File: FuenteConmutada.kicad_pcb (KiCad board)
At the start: 2 copper layers, 50 x 50 mm, 21 parts, among them J1 Conn_01x02_Socket, J2 Conn_01x03_Socket, U1 MT3608

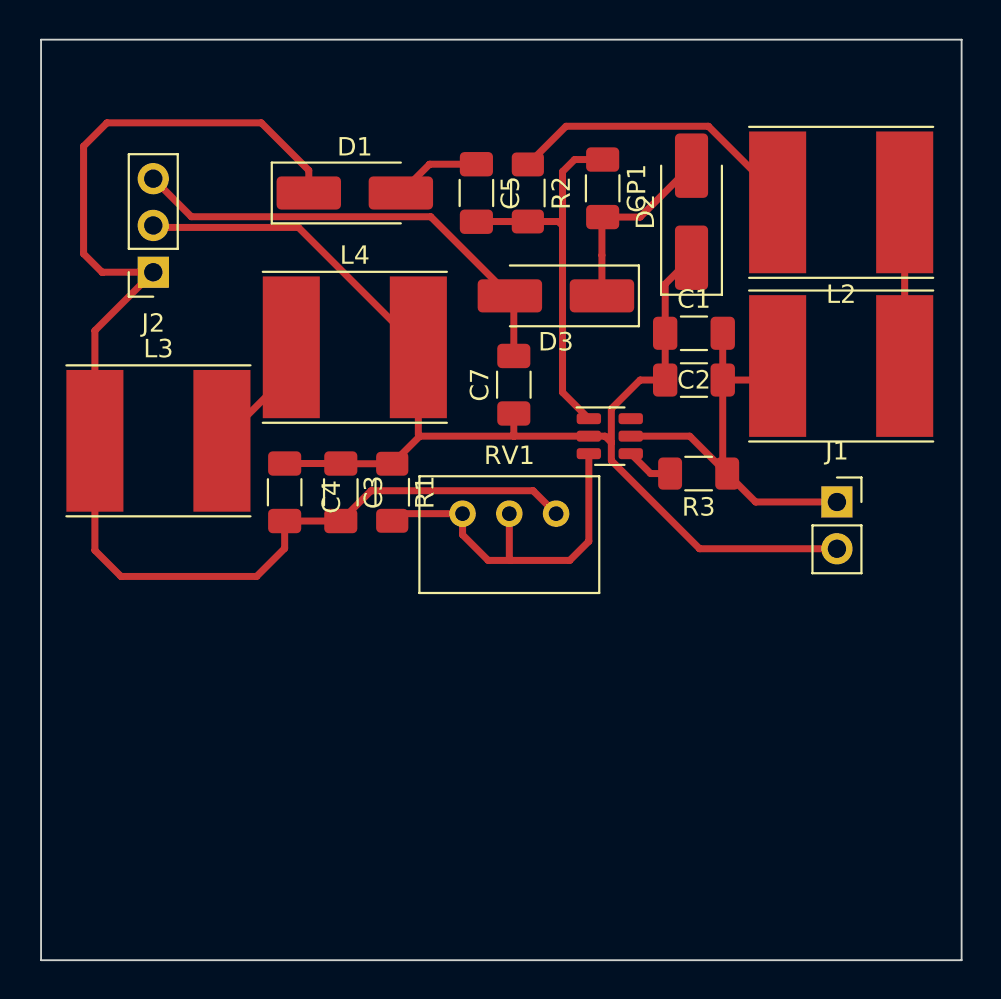
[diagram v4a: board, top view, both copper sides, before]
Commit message: Cambios PCB+Esquematico
Huellas nuevas para inductores, diodos.
Correccion de diodo mal ubicado.
Se añadio R en serie con inductores 3 y 4, capacitor para compensacion, un segundo capacitor para salida Vo-.
Planos de GND, Vin, Vo+ y Vo-. Y tambien se agrandaron algunas pistas.
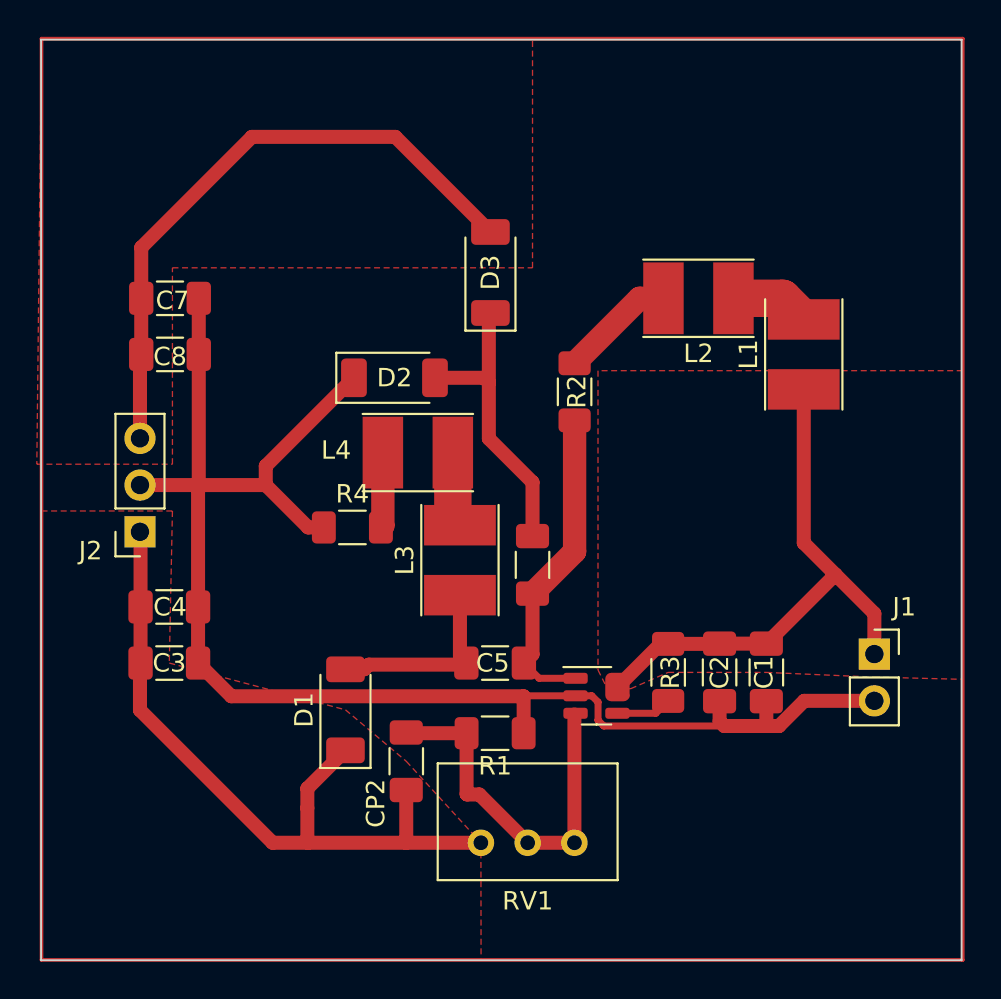
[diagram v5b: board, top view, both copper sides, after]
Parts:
- added C8: 22uF, Capacitor_SMD:C_1206_3216Metric_Pad1.33x1.80mm_HandSolder, F.Cu at (72.0, 93.1)
- added CP2: 22uF, Capacitor_SMD:C_1206_3216Metric_Pad1.33x1.80mm_HandSolder, F.Cu at (84.8, 115.2)
- added R4: R, Resistor_SMD:R_1206_3216Metric_Pad1.30x1.75mm_HandSolder, F.Cu at (81.9, 102.5)
- D1, D2, D3: footprint Diode_SMD:D_SMA_Handsoldering -> Diode_SMD:D_SOD-128
- L1, L2, L3, L4: footprint Inductor_SMD:L_Taiyo-Yuden_NR-80xx_HandSoldering -> Inductor_SMD:L_Taiyo-Yuden_NR-40xx_HandSoldering
- moved D1 28.1 mm to (81.5, 112.4), turned to 90 degrees
- moved C5 25.6 mm to (89.7, 109.9), turned to 0 degrees
- moved CP1 20.8 mm to (91.7, 104.5), turned to 90 degrees
- moved C7 19.3 mm to (72.0, 90.0), turned to 180 degrees
- moved C1 18.8 mm to (104.4, 110.4), turned to 90 degrees
- moved D2 18.5 mm to (84.2, 94.4), turned to 0 degrees
- moved RV1 18.3 mm to (88.9, 119.6), turned to 180 degrees
- moved L3 17.6 mm to (87.8, 104.3), turned to 90 degrees
- moved C2 15.9 mm to (101.9, 110.4), turned to 90 degrees
- moved R1 14.2 mm to (89.7, 113.7), turned to 0 degrees
- moved J2 14.1 mm to (70.4, 102.7)
- moved U1 14.1 mm to (95.2, 111.6)
- moved C3 13.1 mm to (72.0, 109.9), turned to 180 degrees
- moved R2 11.1 mm to (94.0, 95.1)
- moved R3 10.9 mm to (99.1, 110.4), turned to -90 degrees
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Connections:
- L3 pad 1: /Vo+ -> Net-(D1-A)
- L4 pad 2: GND -> Net-(L4-Pad2)
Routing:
- net /Vo+: track 70.5 -> 40.0 mm
- net GND: track 69.6 -> 82.8 mm
- net Net-(L2-Pad2): track 18.7 -> 6.29 mm
- net /Vo-: track 25.4 -> 34.0 mm
- net /Vin: track 23.4 -> 30.8 mm
- net Net-(D1-A): track 4.75 -> 10.5 mm
- net Net-(D2-A): track 10.5 -> 16.2 mm
- net Net-(L1-Pad2): track 8.89 -> 4.30 mm
- net Net-(L4-Pad2): track 0.00 -> 4.11 mm
- net Net-(L3-Pad2): track 7.95 -> 4.10 mm
- net Net-(U1-SW): track 21.2 -> 17.5 mm
- net Net-(U1-FB): track 19.8 -> 20.6 mm
- added copper zone on F.Cu, net /Vin
- added copper zone on F.Cu, net /Vo+
- added copper zone on F.Cu, net /Vo-
- added copper zone on F.Cu, net GND

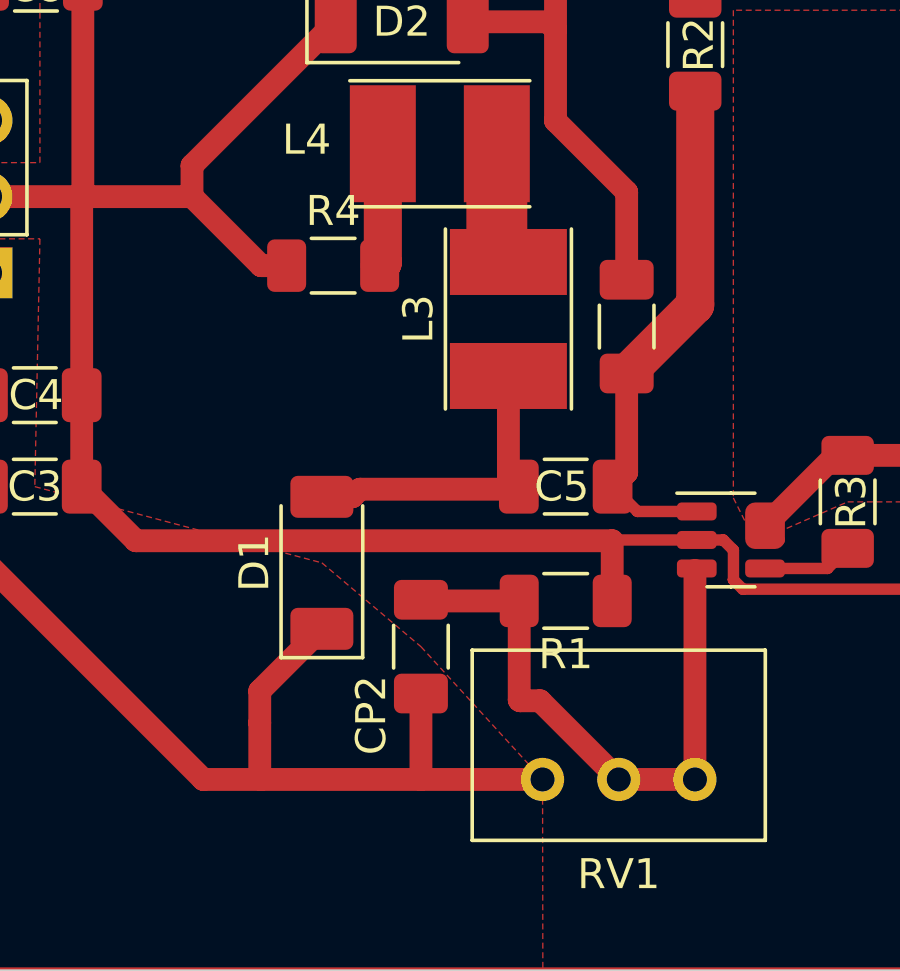
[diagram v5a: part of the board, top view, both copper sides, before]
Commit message: PCB+Esquematico(actualizacion)
Se agrego R en serie con el diodo D1.
Y se habia agregado anteriormente una modificación sobre la huella del regulador.
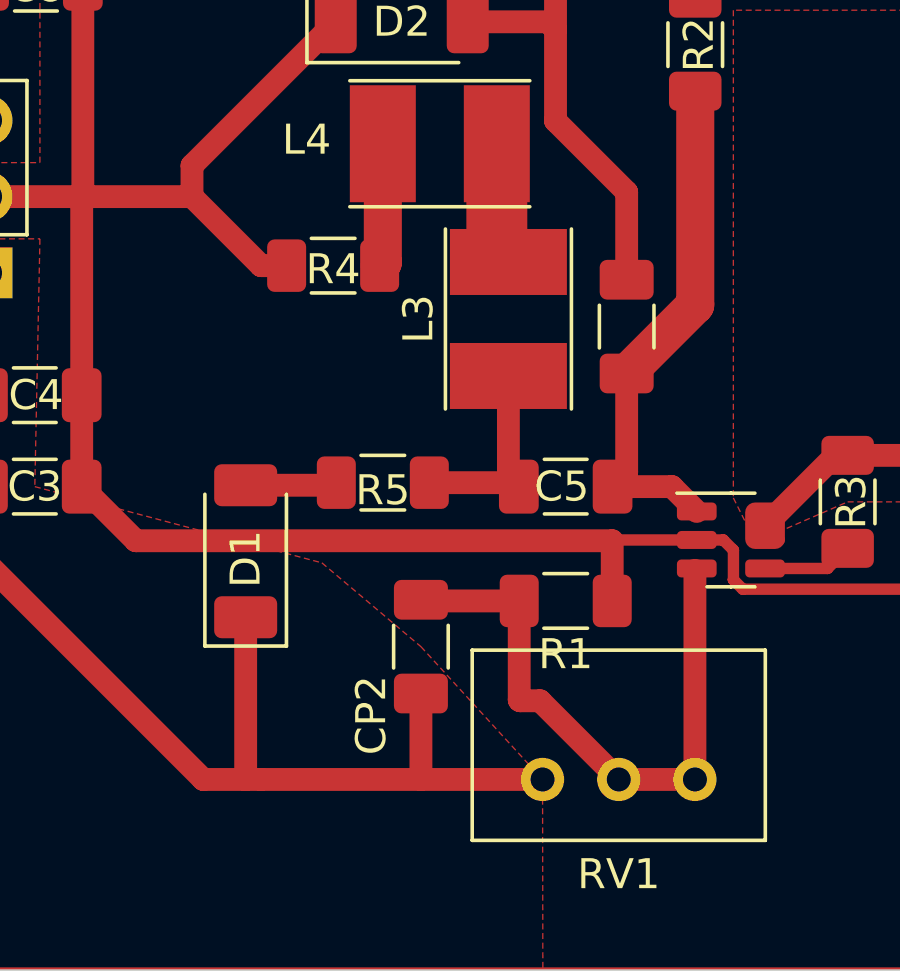
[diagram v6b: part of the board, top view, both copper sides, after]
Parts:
- added R5: R, Resistor_SMD:R_1206_3216Metric_Pad1.30x1.75mm_HandSolder, F.Cu at (83.6, 109.7)
- moved D1 2.57 mm to (79.0, 112.0)
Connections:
- C5 pad 1: Net-(D1-A) -> Net-(C5-Pad1)
- L3 pad 1: Net-(D1-A) -> Net-(C5-Pad1)
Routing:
- net Net-(D1-A): track 10.5 -> 3.06 mm
- net Net-(C5-Pad1): track 0.00 -> 6.99 mm
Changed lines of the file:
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@@
   (net 12 "Net-(L3-Pad2)")
   (net 13 "Net-(L4-Pad2)")
+  (net 14 "Net-(C5-Pad1)")
   (footprint "Capacitor_SMD:C_1206_3216Metric_Pad1.33x1.80mm_HandSolder" (layer "F.Cu")
     (at 91.694 104.526 90)
@@
     (property "ki_keywords" "R res resistor")
     (attr smd)
-    (fp_text reference "R4" (at 0 -1.82) (layer "F.SilkS")
+    (fp_text reference "R4" (at 0 0.122) (layer "F.SilkS")
         (effects (font (size 1 1) (thickness 0.15)))
     )
     (fp_text value "R" (at 0 1.82) (layer "F.Fab")
         (effects (font (size 1 1) (thickness 0.15)))
-    )
-    (fp_text user "${REFERENCE}" (at 0 0) (layer "F.Fab")
-        (effects (font (size 0.8 0.8) (thickness 0.12)))
     )
     (fp_line (start -0.727064 -0.91) (end 0.727064 -0.91)
@@
       (stroke (width 0.1) (type solid)) (layer "F.Fab"))
     (pad "1" smd rect (at -1.9 0 90) (size 2.2 3.9) (layers "F.Cu" "F.Paste" "F.Mask")
-      (net 3 "Net-(D1-A)") (pinfunction "1") (pintype "passive"))
+      (net 14 "Net-(C5-Pad1)") (pinfunction "1") (pintype "passive"))
     (pad "2" smd rect (at 1.9 0 90) (size 2.2 3.9) (layers "F.Cu" "F.Paste" "F.Mask")
       (net 12 "Net-(L3-Pad2)") (pinfunction "2") (pintype "passive"))
@@
   )
   (footprint "Diode_SMD:D_SOD-128" (layer "F.Cu")
-    (at 81.534 112.4 90)
+    (at 78.994 112.014 90)
     (descr "D_SOD-128 (CFP5 SlimSMAW), https://assets.nexperia.com/documents/outline-drawing/SOD128.pdf")
     (tags "D_SOD-128")
@@
     (property "ki_keywords" "diode Schottky")
     (attr smd)
-    (fp_text reference "D1" (at 0 -2.25 90) (layer "F.SilkS")
+    (fp_text reference "D1" (at -0.254 0 90) (layer "F.SilkS")
         (effects (font (size 1 1) (thickness 0.15)))
     )
@@
       (stroke (width 0.1) (type solid)) (layer "F.Fab"))
     (pad "1" smd roundrect (at -1.5625 0) (size 1.325 1.8) (layers "F.Cu" "F.Paste" "F.Mask") (roundrect_rratio 0.188679)
-      (net 3 "Net-(D1-A)") (pintype "passive"))
+      (net 14 "Net-(C5-Pad1)") (pintype "passive"))
     (pad "2" smd roundrect (at 1.5625 0) (size 1.325 1.8) (layers "F.Cu" "F.Paste" "F.Mask") (roundrect_rratio 0.188679)
       (net 7 "Net-(U1-SW)") (pintype "passive"))
@@
     (pad "2" smd roundrect (at 1.55 0 270) (size 1.3 1.75) (layers "F.Cu" "F.Paste" "F.Mask") (roundrect_rratio 0.192308)
       (net 2 "Net-(U1-EN)") (pintype "passive"))
+    (model "${KICAD6_3DMODEL_DIR}/Resistor_SMD.3dshapes/R_1206_3216Metric.wrl"
+      (offset (xyz 0 0 0))
+      (scale (xyz 1 1 1))
+      (rotate (xyz 0 0 0))
+    )
+  )
+  (footprint "Resistor_SMD:R_1206_3216Metric_Pad1.30x1.75mm_HandSolder" (layer "F.Cu")
+    (at 83.566 109.728 180)
+    (descr "Resistor SMD 1206 (3216 Metric), square (rectangular) end terminal, IPC_7351 nominal with elongated pad for handsoldering. (Body size source: IPC-SM-782 page 72, https://www.pcb-3d.com/wordpress/wp-content/uploads/ipc-sm-782a_amendment_1_and_2.pdf), generated with kicad-footprint-generator")
+    (tags "resistor handsolder")
+    (property "Sheetfile" "FuenteConmutada.kicad_sch")
+    (property "Sheetname" "")
+    (property "ki_description" "Resistor")
+    (property "ki_keywords" "R res resistor")
+    (attr smd)
+    (fp_text reference "R5" (at 0 -0.254) (layer "F.SilkS")
+        (effects (font (size 1 1) (thickness 0.15)))
+    )
+    (fp_text value "R" (at 0 1.82) (layer "F.Fab")
+        (effects (font (size 1 1) (thickness 0.15)))
+    )
+    (fp_line (start -0.727064 -0.91) (end 0.727064 -0.91)
+      (stroke (width 0.12) (type solid)) (layer "F.SilkS"))
+    (fp_line (start -0.727064 0.91) (end 0.727064 0.91)
+      (stroke (width 0.12) (type solid)) (layer "F.SilkS"))
+    (fp_line (start -2.45 -1.12) (end 2.45 -1.12)
+      (stroke (width 0.05) (type solid)) (layer "F.CrtYd"))
+    (fp_line (start -2.45 1.12) (end -2.45 -1.12)
+      (stroke (width 0.05) (type solid)) (layer "F.CrtYd"))
+    (fp_line (start 2.45 -1.12) (end 2.45 1.12)
+      (stroke (width 0.05) (type solid)) (layer "F.CrtYd"))
+    (fp_line (start 2.45 1.12) (end -2.45 1.12)
+      (stroke (width 0.05) (type solid)) (layer "F.CrtYd"))
+    (fp_line (start -1.6 -0.8) (end 1.6 -0.8)
+      (stroke (width 0.1) (type solid)) (layer "F.Fab"))
+    (fp_line (start -1.6 0.8) (end -1.6 -0.8)
+      (stroke (width 0.1) (type solid)) (layer "F.Fab"))
+    (fp_line (start 1.6 -0.8) (end 1.6 0.8)
+      (stroke (width 0.1) (type solid)) (layer "F.Fab"))
+    (fp_line (start 1.6 0.8) (end -1.6 0.8)
+      (stroke (width 0.1) (type solid)) (layer "F.Fab"))
+    (pad "1" smd roundrect (at -1.55 0 180) (size 1.3 1.75) (layers "F.Cu" "F.Paste" "F.Mask") (roundrect_rratio 0.192308)
+      (net 14 "Net-(C5-Pad1)") (pintype "passive"))
+    (pad "2" smd roundrect (at 1.55 0 180) (size 1.3 1.75) (layers "F.Cu" "F.Paste" "F.Mask") (roundrect_rratio 0.192308)
+      (net 3 "Net-(D1-A)") (pintype "passive"))
     (model "${KICAD6_3DMODEL_DIR}/Resistor_SMD.3dshapes/R_1206_3216Metric.wrl"
       (offset (xyz 0 0 0))
@@
   (segment (start 99.06 111.918) (end 98.39 112.588) (width 0.381) (layer "F.Cu") (net 2))
   (segment (start 98.39 112.588) (end 96.306 112.588) (width 0.381) (layer "F.Cu") (net 2))
-  (segment (start 82.55 110.2) (end 82.804 109.946) (width 0.762) (layer "F.Cu") (net 3))
-  (segment (start 87.752 106.172) (end 87.752 109.5125) (width 0.762) (layer "F.Cu") (net 3))
-  (segment (start 88.0995 109.86) (end 88.0135 109.946) (width 0.762) (layer "F.Cu") (net 3))
-  (segment (start 81.534 110.2) (end 82.55 110.2) (width 0.762) (layer "F.Cu") (net 3))
-  (segment (start 88.0135 109.946) (end 82.804 109.946) (width 0.762) (layer "F.Cu") (net 3))
-  (segment (start 87.752 109.5125) (end 88.0995 109.86) (width 0.762) (layer "F.Cu") (net 3))
+  (segment (start 81.93 109.814) (end 82.016 109.728) (width 0.762) (layer "F.Cu") (net 3))
+  (segment (start 78.994 109.814) (end 81.93 109.814) (width 0.762) (layer "F.Cu") (net 3))
   (segment (start 110.261 109.372) (end 110.261 107.1695) (width 0.762) (layer "F.Cu") (net 4))
   (segment (start 104.394 108.8055) (end 108.1455 105.054) (width 0.762) (layer "F.Cu") (net 4))
@@
   (segment (start 88.89 119.621) (end 84.836 119.621) (width 0.762) (layer "F.Cu") (net 5))
   (segment (start 84.836 119.621) (end 79.502 119.621) (width 0.762) (layer "F.Cu") (net 5))
-  (segment (start 79.4635 119.5825) (end 79.502 119.621) (width 0.762) (layer "F.Cu") (net 5))
+  (segment (start 78.994 119.621) (end 77.579 119.621) (width 0.762) (layer "F.Cu") (net 5))
+  (segment (start 79.502 119.621) (end 78.994 119.621) (width 0.762) (layer "F.Cu") (net 5))
   (segment (start 70.373 109.89) (end 70.403 109.86) (width 0.762) (layer "F.Cu") (net 5))
-  (segment (start 79.4635 116.6705) (end 79.4635 117.734) (width 0.762) (layer "F.Cu") (net 5))
   (segment (start 70.373 112.415) (end 77.579 119.621) (width 0.762) (layer "F.Cu") (net 5))
   (segment (start 84.836 116.7565) (end 84.836 119.621) (width 0.762) (layer "F.Cu") (net 5))
   (segment (start 70.403 102.763) (end 70.373 102.733) (width 0.762) (layer "F.Cu") (net 5))
-  (segment (start 81.534 114.6) (end 79.4635 116.6705) (width 0.762) (layer "F.Cu") (net 5))
+  (segment (start 78.994 114.214) (end 78.994 119.621) (width 0.762) (layer "F.Cu") (net 5))
   (segment (start 70.403 109.86) (end 70.403 106.812) (width 0.762) (layer "F.Cu") (net 5))
-  (segment (start 79.4635 117.734) (end 79.4635 119.5825) (width 0.762) (layer "F.Cu") (net 5))
   (segment (start 70.373 112.415) (end 70.373 109.89) (width 0.762) (layer "F.Cu") (net 5))
-  (segment (start 79.502 119.621) (end 77.579 119.621) (width 0.762) (layer "F.Cu") (net 5))
   (segment (start 70.403 106.812) (end 70.403 102.763) (width 0.762) (layer "F.Cu") (net 5))
   (segment (start 93.97 112.649) (end 93.97 119.621) (width 0.762) (layer "F.Cu") (net 6))
@@
   (segment (start 84.8745 113.67) (end 84.836 113.6315) (width 0.762) (layer "F.Cu") (net 6))
   (segment (start 91.694 109.3905) (end 91.694 106.0885) (width 0.762) (layer "F.Cu") (net 7))
+  (segment (start 93.203 109.86) (end 94.031 110.688) (width 0.762) (layer "F.Cu") (net 7))
   (segment (start 93.98 103.8025) (end 93.98 96.678) (width 1.27) (layer "F.Cu") (net 7))
+  (segment (start 91.2245 109.86) (end 93.203 109.86) (width 0.762) (layer "F.Cu") (net 7))
   (segment (start 91.694 106.0885) (end 93.98 103.8025) (width 1.27) (layer "F.Cu") (net 7))
-  (segment (start 94.031 110.688) (end 92.0525 110.688) (width 0.381) (layer "F.Cu") (net 7))
-  (segment (start 92.0525 110.688) (end 91.2245 109.86) (width 0.381) (layer "F.Cu") (net 7))
   (segment (start 93.954 96.704) (end 93.98 96.678) (width 0.381) (layer "F.Cu") (net 7))
   (segment (start 91.2245 109.86) (end 91.694 109.3905) (width 0.762) (layer "F.Cu") (net 7))
@@
   (segment (start 83.566 98.43) (end 83.566 102.388) (width 1.27) (layer "F.Cu") (net 13))
   (segment (start 83.566 102.388) (end 83.46 102.494) (width 1.27) (layer "F.Cu") (net 13))
+  (segment (start 87.752 106.172) (end 87.752 109.5125) (width 0.762) (layer "F.Cu") (net 14))
+  (segment (start 88.0995 109.86) (end 88.0135 109.946) (width 0.762) (layer "F.Cu") (net 14))
+  (segment (start 87.9675 109.728) (end 88.0995 109.86) (width 0.762) (layer "F.Cu") (net 14))
+  (segment (start 85.116 109.728) (end 87.9675 109.728) (width 0.762) (layer "F.Cu") (net 14))
+  (segment (start 87.752 109.5125) (end 88.0995 109.86) (width 0.762) (layer "F.Cu") (net 14))
   (zone (net 4) (net_name "/Vin") (layer "F.Cu") (hatch edge 0.5)
     (priority 2)
